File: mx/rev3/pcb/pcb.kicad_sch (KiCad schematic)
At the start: 277 parts, among them J1 Conn_01x03, J2 Conn_01x03, J3 Conn_01x03, J4 Conn_01x03, J5 Conn_01x03, J6 Conn_01x03, J7 Conn_01x03, J8 Conn_01x03, Q1 MMBT3904, Q2 MMBT3904, Q3 MMBT3904, SW1 SW_DIP_x01_XKB_TS_2030, SW2 SW_DIP_x01_XKB_TS_2030, U1 IS31FL3731-QF

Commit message: M  .gitignore M  giri-kicad-lib/switches.kicad_sym A  giri-kicad-lib/switches_lib.pretty/RP2040_Stamp.kicad_mod A  giri-kicad-lib/switches_lib.pretty/SW_B3U-3000P.kicad_mod M  lopro/8rows/pcb/pcb.kicad_sch A  mx/rev3/.border.py.swp A  mx/rev3/.build.py.swp A  mx/rev3/build.py M  mx/rev3/pcb/pcb.kicad_pcb M  mx/rev3/pcb/pcb.kicad_prl M  mx/rev3/pcb/pcb.kicad_sch D  mx/rev3/place.py A  mx/rev3/test.py D  rp2040backpack/pcb/jlcpcb/gerbers1p2/pcb-B_Cu.gbl D  rp2040backpack/pcb/jlcpcb/gerbers1p2/pcb-B_Mask.gbs D  rp2040backpack/pcb/jlcpcb/gerbers1p2/pcb-B_Paste.gbp D  rp2040backpack/pcb/jlcpcb/gerbers1p2/pcb-B_Silkscreen.gbo D  rp2040backpack/pcb/jlcpcb/gerbers1p2/pcb-Edge_Cuts.gm1 D  rp2040backpack/pcb/jlcpcb/gerbers1p2/pcb-F_Cu.gtl D  rp2040backpack/pcb/jlcpcb/gerbers1p2/pcb-F_Mask.gts D  rp2040backpack/pcb/jlcpcb/gerbers1p2/pcb-F_Paste.gtp D  rp2040backpack/pcb/jlcpcb/gerbers1p2/pcb-F_Silkscreen.gto D  rp2040backpack/pcb/jlcpcb/gerbers1p2/pcb-NPTH-drl_map.gbr D  rp2040backpack/pcb/jlcpcb/gerbers1p2/pcb-NPTH.drl D  rp2040backpack/pcb/jlcpcb/gerbers1p2/pcb-PTH-drl_map.gbr D  rp2040backpack/pcb/jlcpcb/gerbers1p2/pcb-PTH.drl R  rp2040backpack/pickle.py -> rp2040stamp/pickle.py R  rp2040backpack/pcb/.gitignore -> rp2040stamp/rev1/pcb/.gitignore R  rp2040backpack/pcb/LED-Driver.kicad_sch -> rp2040stamp/rev1/pcb/LED-Driver.kicad_sch R  rp2040backpack/pcb/fp-lib-table -> rp2040stamp/rev1/pcb/fp-lib-table R  rp2040backpack/pcb/pcb-b.jpg -> rp2040stamp/rev1/pcb/pcb-b.jpg R  rp2040backpack/pcb/pcb.jpg -> rp2040stamp/rev1/pcb/pcb.jpg R  rp2040backpack/pcb/pcb.kicad_pcb -> rp2040stamp/rev1/pcb/pcb.kicad_pcb R  rp2040backpack/pcb/pcb.kicad_prl -> rp2040stamp/rev1/pcb/pcb.kicad_prl R  rp2040backpack/pcb/pcb.kicad_pro -> rp2040stamp/rev1/pcb/pcb.kicad_pro R  rp2040backpack/pcb/pcb.kicad_sch -> rp2040stamp/rev1/pcb/pcb.kicad_sch R  rp2040backpack/pcb/sym-lib-table -> rp2040stamp/rev1/pcb/sym-lib-table A  rp2040stamp/rev2/pcb/.gitignore A  rp2040stamp/rev2/pcb/LED-Driver.kicad_sch A  r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
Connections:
- net +3V3: no longer C1.2, C2.1, C3.1
- net +5V: now also C1.2, C2.1, C3.1
- net ~{SDB}: now also Jrp1.H5 (GPIO15)
- no-connect marks 40 -> 39
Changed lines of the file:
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@@
   (no_connect (at 111.76 281.94))
   (no_connect (at 29.21 350.52))
-  (no_connect (at 115.57 246.38))
   (no_connect (at 54.61 365.76))
   (no_connect (at 66.04 236.22))
@@
     (stroke (width 0) (type default))
   )
-  (wire (pts (xy 111.76 246.38) (xy 115.57 246.38))
-    (stroke (width 0) (type default))
-  )
   (wire (pts (xy 510.54 269.24) (xy 510.54 273.05))
     (stroke (width 0) (type default))
@@
     (stroke (width 0) (type default))
   )
+  (wire (pts (xy 111.76 246.38) (xy 119.38 246.38))
+    (stroke (width 0) (type default))
+  )
   (wire (pts (xy 422.91 50.8) (xy 426.72 50.8))
     (stroke (width 0) (type default))
@@
     (effects (font (size 1.27 1.27)) (justify right bottom))
   )
+  (label "~{SDB}" (at 119.38 246.38 0) (fields_autoplaced)
+    (effects (font (size 1.27 1.27)) (justify left bottom))
+  )
   (label "COL15" (at 115.57 243.84 0) (fields_autoplaced)
     (effects (font (size 1.27 1.27)) (justify left bottom))
@@
     )
   )
-  (symbol (lib_id "power:+3V3") (at 538.48 260.35 0) (unit 1)
-    (in_bom yes) (on_board yes) (dnp no)
-    (property "Reference" "#PWR065" (at 538.48 264.16 0)
-      (effects (font (size 1.27 1.27)) hide)
-    )
-    (property "Value" "+3V3" (at 538.861 255.9558 0)
-      (effects (font (size 1.27 1.27)))
-    )
-    (property "Footprint" "" (at 538.48 260.35 0)
-      (effects (font (size 1.27 1.27)) hide)
-    )
-    (property "Datasheet" "" (at 538.48 260.35 0)
-      (effects (font (size 1.27 1.27)) hide)
-    )
-    (pin "1")
-    (instances
-      (project "pcb"
-        (path "/fc5aba81-0b5f-4276-86c2-3faa68e4e536"
-          (reference "#PWR065") (unit 1)
-        )
-      )
-    )
-  )
   (symbol (lib_id "giri:Rgr") (at 487.68 137.16 180) (unit 1)
     (in_bom yes) (on_board yes) (dnp no) (fields_autoplaced)
@@
         )
       )
+    )
+  )
+  (symbol (lib_id "power:+5V") (at 538.48 260.35 0) (unit 1)
+    (in_bom yes) (on_board yes) (dnp no) (fields_autoplaced)
+    (property "Reference" "#PWR079" (at 538.48 264.16 0)
+      (effects (font (size 1.27 1.27)) hide)
+    )
+    (property "Value" "+5V" (at 538.48 256.7742 0)
+      (effects (font (size 1.27 1.27)))
+    )
+    (property "Footprint" "" (at 538.48 260.35 0)
+      (effects (font (size 1.27 1.27)) hide)
+    )
+    (property "Datasheet" "" (at 538.48 260.35 0)
+      (effects (font (size 1.27 1.27)) hide)
+    )
+    (pin "1")
+    (instances
+      (project "pcb"
+        (path "/fc5aba81-0b5f-4276-86c2-3faa68e4e536"
+          (reference "#PWR079") (unit 1)
+        )
+      )

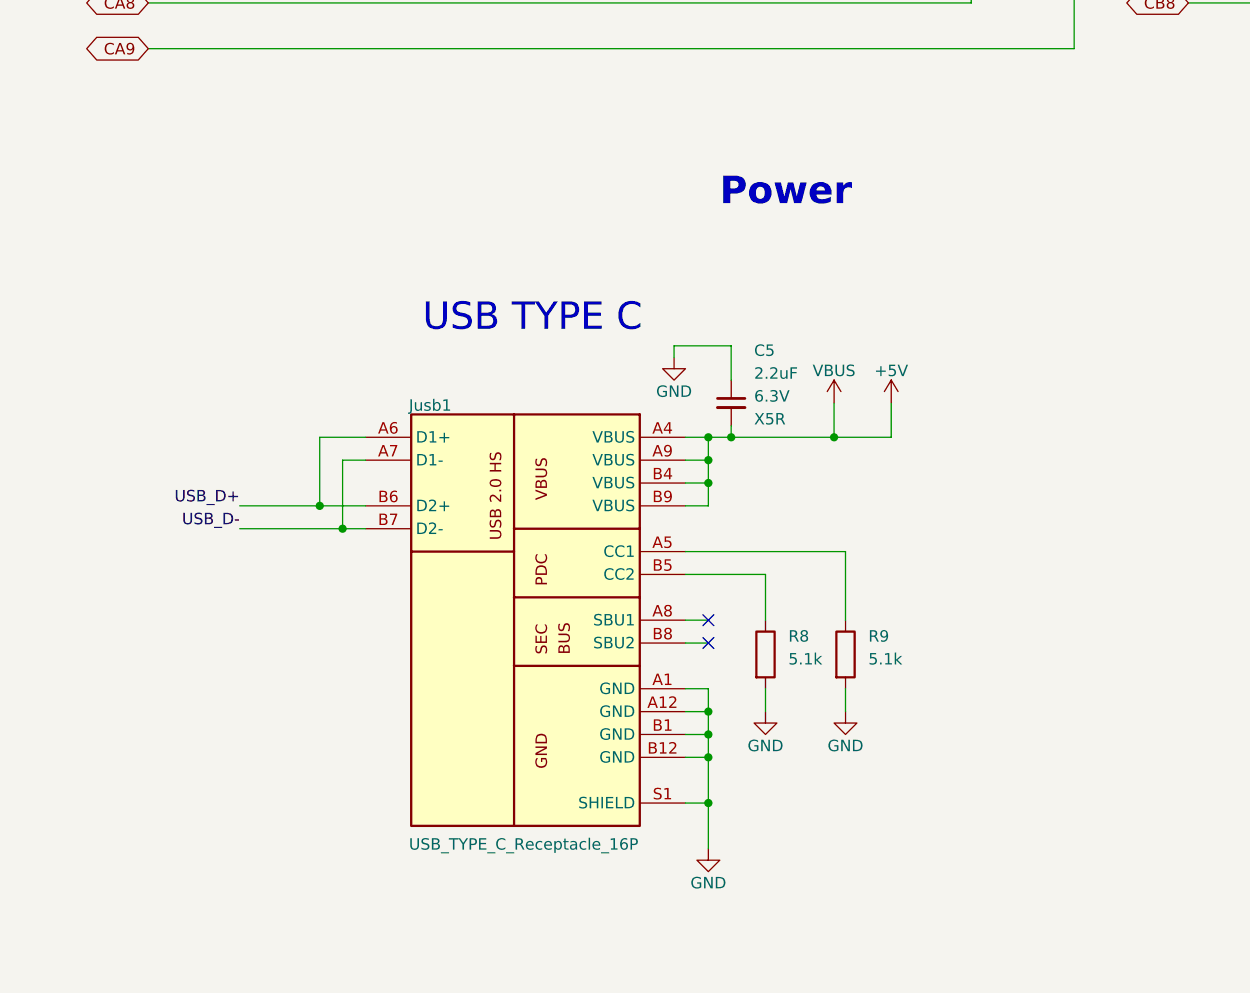
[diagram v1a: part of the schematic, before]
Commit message: M mx/rev3/border.py M  mx/rev3/pcb/pcb.kicad_pcb M  mx/rev3/pcb/pcb.kicad_prl M  mx/rev3/pcb/pcb.kicad_sch RM mx/rev3/build.py -> mx/rev3/place.py
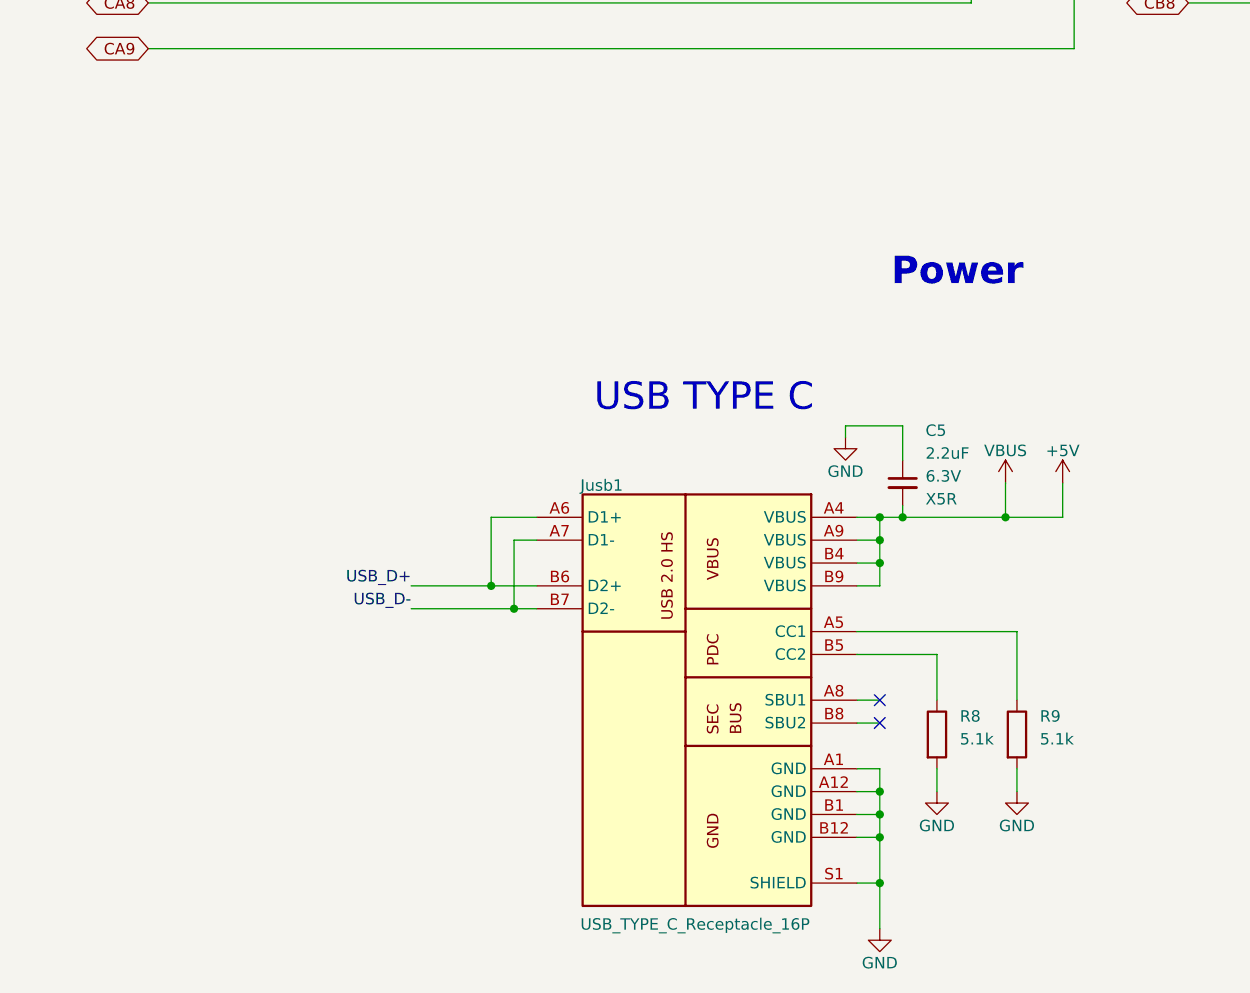
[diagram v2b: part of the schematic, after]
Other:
- moved on the sheet: C5, Jusb1, R8, R9

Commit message: M giri-kicad-lib/switches.kicad_sym  M giri-kicad-lib/switches_lib.pretty/PGA2040_SMT_WITH_SLOT.kicad_mod M  mx/rev3/border.py M  mx/rev3/pcb/pcb.kicad_pcb M  mx/rev3/pcb/pcb.kicad_prl M  mx/rev3/pcb/pcb.kicad_sch M  mx/rev3/place.py ?? giri-kicad-lib/switches_lib.pretty/ALS-PT19.kicad_mod ?? giri-kicad-lib/switches_lib.pretty/Debug_PinHeader_1x06_P2.00mm_Vertical.kicad_mod ?? giri-kicad-lib/switches_lib.pretty/PGA2040_SMT_NO_SLOT.kicad_mod ?? giri-kicad-lib/switches_lib.pretty/PinHeader_1x02_P2.54mm_Vertical.kicad_mod ?? giri-kicad-lib/switches_lib.pretty/TEMT6000-sensor.kicad_mod ?? giri-kicad-lib/switches_lib.pretty/mouse-bite-2mm-slot.kicad_mod
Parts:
- removed J1, J2, J3, J4, J5, J6, J7, J8: Conn_01x03, giri:PinHeader_1x03_P2.54mm_Vertical, symbol Connector:Conn_01x03_Socket
- added Ba1: Conn_01x02_Socket, giri:PinHeader_1x02_P2.54mm_Vertical, symbol giri:Battery
- added J1: Conn_01x06_Socket, giri:Debug_PinHeader_1x06_P2.00mm_Vertical, symbol Connector:Conn_01x06_Socket
- added J2: Conn_01x07_Pin, Connector_JST:JST_SH_SM06B-SRSS-TB_1x06-1MP_P1.00mm_Horizontal, symbol giri:JST_Conn_01x07_Pin
- added JP1: SolderJumper_2_Bridged, Jumper:SolderJumper-2_P1.3mm_Bridged2Bar_RoundedPad1.0x1.5mm, symbol Jumper:SolderJumper_2_Bridged
- added JP2: SolderJumper_2_Open, Jumper:SolderJumper-2_P1.3mm_Open_TrianglePad1.0x1.5mm, symbol Jumper:SolderJumper_2_Open
- added R10: 10k, RP2040_Minimal:R_0603_1608Metric_Pad0.98x0.95mm_HandSolder, symbol Device:R
- added Sens1, Sens2: ~, giri:ALS-PT19, symbol giri:Sensor_Ambient_Light
- H1, H2, H3, H4, H5, H6, H7, H8: footprint giri:MountingHole_2.2mm_M2_ISO7380_Pad -> giri:SMTSO_M2
- Jrp1: footprint giri:PGA2040_SMT_WITH_SLOT -> giri:PGA2040_SMT_NO_SLOT
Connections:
- net +3V3: now also J1.4 (Pin_4), J2.4 (Pin_4), Sens1.1 (C), Sens2.1 (C)
- net COL1: now also Jrp1.C8 (GPIO27/ADC1); no longer Jrp1.B1 (GPIO0)
- net COL10: now also Jrp1.H6 (GPIO17); no longer Jrp1.G1 (GPIO9)
- net COL11: now also Jrp1.G5 (GPIO16); no longer Jrp1.H2 (GPIO10)
- net COL12: now also Jrp1.H5 (GPIO15); no longer Jrp1.H3 (GPIO11)
- net COL13: now also Jrp1.G4 (GPIO14); no longer Jrp1.G3 (GPIO12)
- net COL15: now also Jrp1.G3 (GPIO12); no longer Jrp1.G4 (GPIO14)
- net COL2: now also Jrp1.D7 (GPIO26/ADC0); no longer Jrp1.C1 (GPIO1)
- net COL3: now also Jrp1.D8 (GPIO25); no longer Jrp1.C2 (GPIO2)
- net COL4: now also Jrp1.E7 (GPIO24); no longer Jrp1.D1 (GPIO3)
- net COL5: now also Jrp1.E8 (GPIO23); no longer Jrp1.D2 (GPIO4)
- net COL6: now also Jrp1.F7 (GPIO22); no longer Jrp1.E1 (GPIO5)
- net COL7: now also Jrp1.F8 (GPIO21); no longer Jrp1.E2 (GPIO6)
- net COL8: now also Jrp1.G8 (GPIO20); no longer Jrp1.F1 (GPIO7)
- net COL9: now also Jrp1.G6 (GPIO18); no longer Jrp1.F2 (GPIO8)
- net GND: now also Ba1.1 (Pin_1), J1.2 (Pin_2), J2.2 (Pin_2), J2.MP (Pin_7), R10.2
- net ROW1: now also Jrp1.C7 (GPIO28/ADC2); no longer Jrp1.G6 (GPIO18)
- net ROW3: now also Jrp1.H3 (GPIO11); no longer Jrp1.G8 (GPIO20)
- net ROW4: now also Jrp1.H2 (GPIO10); no longer Jrp1.F8 (GPIO21)
- net ROW5: now also Jrp1.G1 (GPIO9); no longer Jrp1.F7 (GPIO22)
- net RUN: now also J1.5 (Pin_5), J2.5 (Pin_5)
- net SCL: now also Jrp1.F1 (GPIO7); no longer Jrp1.H6 (GPIO17)
- net SDA: now also Jrp1.E2 (GPIO6); no longer Jrp1.G5 (GPIO16)
- net ~{SDB}: now also Jrp1.F2 (GPIO8); no longer Jrp1.H5 (GPIO15)
- net ~{USB_BOOT}: now also JP2.2 (B)
- net SWCLK: now reaches Jrp1.B5 (SWCLK)
- net SWCLK: now also J1.1 (Pin_1), J2.1 (Pin_1)
- net SWDIO: now reaches Jrp1.B6 (SWDIO)
- net SWDIO: now also J1.3 (Pin_3), J2.3 (Pin_3)
- net SENSOR: now reaches Jrp1.B8 (GPIO29/ADC3)
- net SENSOR: now also R10.1, Sens1.2 (E), Sens2.2 (E)
- net +5V renamed VBUS
- net VBUS: now also J1.6 (Pin_6), J2.6 (Pin_6), JP1.1 (A); no longer Jrp1.A2 (VBUS)
- new net: JP1.2 (B), Jrp1.A2 (VBUS)
- new net BATT: Ba1.2 (Pin_2), JP2.1 (A)
- no-connect marks 39 -> 12
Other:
- note added: "Ambient Light Sensor"
- note added: "Battery"
- note added: "Daughter Board"
- note added: "Debug"
- note removed: "Dummy Conn"
- moved on the sheet: C5, H1, H2, H3, H4, H5, H6, H7, H8, Hs1, Hs10, Hs11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

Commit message: M giri-kicad-lib/switches.kicad_sym  M giri-kicad-lib/switches_lib.pretty/Gateron_1u.kicad_mod  M giri-kicad-lib/switches_lib.pretty/Gateron_Sw_1u.kicad_mod  M giri-kicad-lib/switches_lib.pretty/PGA2040_SMT_WITH_SLOT.kicad_mod  M giri-kicad-lib/switches_lib.pretty/SW_B3U-3000P.kicad_mod M  mx/rev3/border.py M  mx/rev3/pcb/fp-lib-table M  mx/rev3/pcb/pcb.kicad_pcb M  mx/rev3/pcb/pcb.kicad_prl M  mx/rev3/pcb/pcb.kicad_pro M  mx/rev3/pcb/pcb.kicad_sch M  mx/rev3/place.py M  mx/rev3/switch-plate/switch-plate.kicad_pcb M  mx/rev3/switch-plate/switch-plate.kicad_prl M  mx/rev3/switch-plate/switch-plate.kicad_pro M  mx/rev3/switch-plate/switch-plate.kicad_sch M  mx/rev3/wrist-washer/wrist-washer.kicad_pcb M  mx/rev3/wrist-washer/wrist-washer.kicad_prl M  mx/rev3/wrist-washer/wrist-washer.kicad_pro M  mx/rev3/wrist-washer/wrist-washer.kicad_sch ?? giri-kicad-lib/switches_lib.pretty/ALS-PT19.kicad_mod ?? giri-kicad-lib/switches_lib.pretty/Debug_PinHeader_1x06_P2.00mm_Vertical.kicad_mod ?? giri-kicad-lib/switches_lib.pretty/Debug_PinHeader_1x06_P2.54mm_Vertical.kicad_mod ?? giri-kicad-lib/switches_lib.pretty/Gateron_1.25.kicad_mod ?? giri-kicad-lib/switches_lib.pretty/Gateron_1.25u_v2.kicad_mod ?? giri-kicad-lib/switches_lib.pretty/Gateron_1u_v2.kicad_mod ?? giri-kicad-lib/switches_lib.pretty/Gateron_2.25u.kicad_mod ?? giri-kicad-lib/switches_lib.pretty/Gateron_2u.kicad_mod ?? giri-kicad-lib/switches_lib.pretty/Gateron_2u_v2.kicad_mod ?? giri-kicad-lib/switches_lib.pretty/MountingHole_2.2mm_M2_NoPad.kicad_mod ?? giri-kicad-lib/switches_lib.pretty/PGA2040_SMT_NO_SLOT.kicad_mod ?? giri-kicad-lib/switches_lib.pretty/PinHeader_1x02_P2.54mm_Vertical.kicad_mod ?? giri-kicad-lib/switches_lib.pretty/Switch_Cutout_MX_2.25u.kicad_mod ?? giri-kicad-lib/switches_lib.pretty/Switch_Cutout_MX_2u.kicad_mod ?? giri-kicad-lib/switches_lib.pretty/TEMT6000-sensor.kicad_mod ?? giri-kicad-lib/switches_lib.pretty/mouse-bite-2mm-slot.kicad_mod ?? "resources/1x2 stabilizer.png" ?? resources/Keymodule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
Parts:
- removed J2: Conn_01x07_Pin, Connector_JST:JST_SH_SM06B-SRSS-TB_1x06-1MP_P1.00mm_Horizontal, symbol giri:JST_Conn_01x07_Pin
- added F1: 500ma, Fuse:Fuse_0603_1608Metric, symbol Device:Polyfuse_Small
- added JP2, JP3: SolderJumper_2_Open, Jumper:SolderJumper-2_P1.3mm_Open_TrianglePad1.0x1.5mm, symbol Jumper:SolderJumper_2_Open
- J1: footprint giri:Debug_PinHeader_1x06_P2.00mm_Vertical -> giri:Debug_PinHeader_1x06_P2.54mm_Vertical
- S1, S10, S11, S12, S13, S14, S15, S2, S3, S4, S5, S6, S7, S8, S9: footprint giri:Gateron_1u -> giri:Gateron_1u_v2
- S10: footprint giri:Gateron_1u -> giri:Gateron_1.25u_v2
- S10, S15: footprint giri:Gateron_1u -> giri:Gateron_2u_v2
- SW1, SW2: footprint RP2040_Minimal:SW_XKB_TS_2030 -> giri:SW_B3U-3000P
- Sens2: footprint giri:ALS-PT19 -> giri:TEMT6000-sensor
- renumbered JP2 to JP4
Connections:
- net GND: now also J1.1 (Pin_1); no longer J1.2 (Pin_2)
- net SWCLK: now also J1.2 (Pin_2); no longer J1.1 (Pin_1)
- net VBUS: now also Jrp1.A2 (VBUS); no longer C1.2, C2.1, C3.1, J1.6 (Pin_6), S1.1 (IR_A), S1.1 (IR_A), S1.1 (IR_A), S1.1 (IR_A), S1.1 (IR_A), S2.1 (IR_A), S2.1 (IR_A), S2.1 (IR_A), S2.1 (IR_A), S2.1 (IR_A), S3.1 (IR_A), S3.1 (IR_A), S3.1 (IR_A), S3.1 (IR_A), S3.1 (IR_A), S4.1 (IR_A), S4.1 (IR_A), S4.1 (IR_A), S4.1 (IR_A), S4.1 (IR_A), S5.1 (IR_A), S5.1 (IR_A), S5.1 (IR_A), S5.1 (IR_A), U1.2 (VCC)
- net at JP1.2 (B): now also F1.1; no longer Jrp1.A2 (VBUS)
- net at Jrp1.B1 (GPIO0): now also JP2.1 (A)
- net at Jrp1.C1 (GPIO1): now also JP3.1 (A)
- new net +5V: C1.2, C2.1, C3.1, F1.2, JP2.2 (B), S1.1 (IR_A), S1.1 (IR_A), S1.1 (IR_A), S1.1 (IR_A), S1.1 (IR_A), S2.1 (IR_A), S2.1 (IR_A), S2.1 (IR_A), S2.1 (IR_A), S2.1 (IR_A), S3.1 (IR_A), S3.1 (IR_A), S3.1 (IR_A), S3.1 (IR_A), S3.1 (IR_A), S4.1 (IR_A), S4.1 (IR_A), S4.1 (IR_A), S4.1 (IR_A), S4.1 (IR_A), S5.1 (IR_A), S5.1 (IR_A), S5.1 (IR_A), S5.1 (IR_A), U1.2 (VCC)
- new net VDDH: J1.6 (Pin_6), JP3.2 (B)
- no-connect marks 12 -> 10
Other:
- moved on the sheet: JP1
